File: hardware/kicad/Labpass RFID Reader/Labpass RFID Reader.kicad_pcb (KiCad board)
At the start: 2 copper layers, 74 x 74 mm, 59 parts, among them J1 Conn_01x03_Male, J2 Conn_01x08, J3 Conn_01x02, U1 adafruit_huzzah_32, U2 LM393, U3 LM324, U4 MFRC522, Y1 27.12 MHz

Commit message: Add terminal block for gpio to ext relay
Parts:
- added J4: Conn_01x02, Capstone Footprint Library:Anytek NQ, F.Cu at (154.6, 125.9)
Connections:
- net /Indicators/buzzer renamed /Indicators/BUZZER
- U1 pad 22: unconnected-(U1-Pad22) -> /Indicators/EXT_RELAY
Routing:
- net /Indicators/EXT_RELAY: track 0.00 -> 56.3 mm

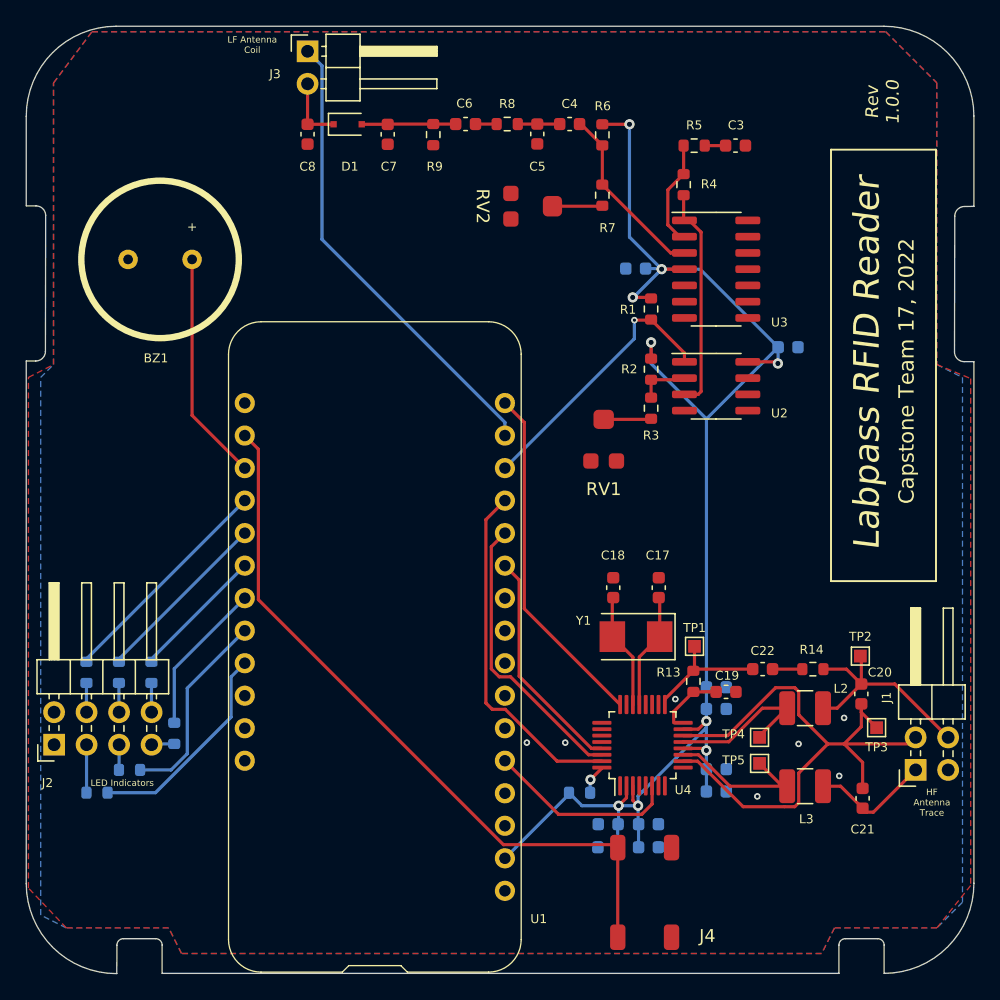
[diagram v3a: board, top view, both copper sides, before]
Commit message: Add back the mounting holes
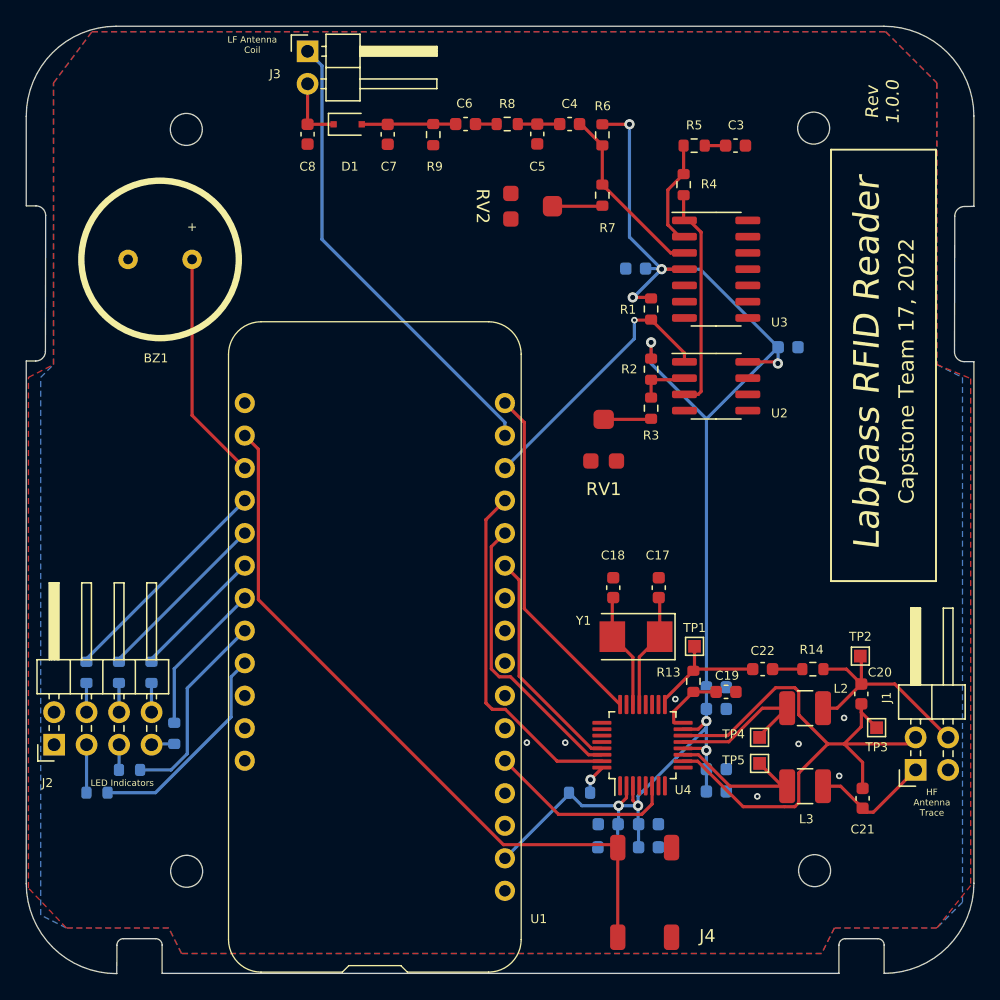
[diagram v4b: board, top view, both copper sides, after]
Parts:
- added REF**: MountingHole_2.5mm, MountingHole:MountingHole_2.5mm, F.Cu at (167.9, 124.2)
- added REF**: MountingHole_2.5mm, MountingHole:MountingHole_2.5mm, F.Cu at (118.8, 124.2)
- added REF**: MountingHole_2.5mm, MountingHole:MountingHole_2.5mm, F.Cu at (118.8, 66.3)
- added REF**: MountingHole_2.5mm, MountingHole:MountingHole_2.5mm, F.Cu at (167.8, 66.2)
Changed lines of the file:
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@@
     )
+  )
+  (footprint "MountingHole:MountingHole_2.5mm" (layer "F.Cu")
+    (at 167.875 124.2)
+    (descr "Mounting Hole 2.5mm, no annular")
+    (tags "mounting hole 2.5mm no annular")
+    (attr exclude_from_pos_files exclude_from_bom)
+    (fp_text reference "REF**" (at 0 -3.5) (layer "F.SilkS") hide
+      (effects (font (size 1 1) (thickness 0.15)))
+    )
+    (fp_text value "MountingHole_2.5mm" (at 0 3.5) (layer "F.Fab")
+      (effects (font (size 1 1) (thickness 0.15)))
+    )
+    (fp_text user "${REFERENCE}" (at 0 0) (layer "F.Fab")
+      (effects (font (size 1 1) (thickness 0.15)))
+    )
+    (fp_circle (center 0 0) (end 2.5 0) (layer "Cmts.User") (width 0.15) (fill none))
+    (fp_circle (center 0 0) (end 2.75 0) (layer "F.CrtYd") (width 0.05) (fill none))
+    (pad "" np_thru_hole circle (at 0 0) (size 2.5 2.5) (drill 2.5) (layers *.Cu *.Mask))
   )
   (footprint "Capstone Footprint Library:buzzer" (layer "F.Cu")
@@
     )
   )
+  (footprint "MountingHole:MountingHole_2.5mm" (layer "F.Cu")
+    (at 118.825 124.25)
+    (descr "Mounting Hole 2.5mm, no annular")
+    (tags "mounting hole 2.5mm no annular")
+    (attr exclude_from_pos_files exclude_from_bom)
+    (fp_text reference "REF**" (at 0 -3.5) (layer "F.SilkS") hide
+      (effects (font (size 1 1) (thickness 0.15)))
+    )
+    (fp_text value "MountingHole_2.5mm" (at 0 3.5) (layer "F.Fab")
+      (effects (font (size 1 1) (thickness 0.15)))
+    )
+    (fp_text user "${REFERENCE}" (at 0 0) (layer "F.Fab")
+      (effects (font (size 1 1) (thickness 0.15)))
+    )
+    (fp_circle (center 0 0) (end 2.5 0) (layer "Cmts.User") (width 0.15) (fill none))
+    (fp_circle (center 0 0) (end 2.75 0) (layer "F.CrtYd") (width 0.05) (fill none))
+    (pad "" np_thru_hole circle (at 0 0) (size 2.5 2.5) (drill 2.5) (layers *.Cu *.Mask))
+  )
   (footprint "Capstone Footprint Library:Anytek NQ" (layer "F.Cu")
     (at 154.6 125.9 -90)
@@
       (rotate (xyz 0 0 0))
     )
+  )
+  (footprint "MountingHole:MountingHole_2.5mm" (layer "F.Cu")
+    (at 118.8 66.3)
+    (descr "Mounting Hole 2.5mm, no annular")
+    (tags "mounting hole 2.5mm no annular")
+    (attr exclude_from_pos_files exclude_from_bom)
+    (fp_text reference "REF**" (at 0 -3.5) (layer "F.SilkS") hide
+      (effects (font (size 1 1) (thickness 0.15)))
+    )
+    (fp_text value "MountingHole_2.5mm" (at 0 3.5) (layer "F.Fab")
+      (effects (font (size 1 1) (thickness 0.15)))
+    )
+    (fp_text user "${REFERENCE}" (at 0 0) (layer "F.Fab")
+      (effects (font (size 1 1) (thickness 0.15)))
+    )
+    (fp_circle (center 0 0) (end 2.5 0) (layer "Cmts.User") (width 0.15) (fill none))
+    (fp_circle (center 0 0) (end 2.75 0) (layer "F.CrtYd") (width 0.05) (fill none))
+    (pad "" np_thru_hole circle (at 0 0) (size 2.5 2.5) (drill 2.5) (layers *.Cu *.Mask))
   )
   (footprint "Resistor_SMD:R_0603_1608Metric" (layer "F.Cu")
@@
       (net 29 "/labpass_rf_13.56M/TX1") (pinfunction "1") (pintype "passive"))
   )
+  (footprint "MountingHole:MountingHole_2.5mm" (layer "F.Cu")
+    (at 167.8 66.2)
+    (descr "Mounting Hole 2.5mm, no annular")
+    (tags "mounting hole 2.5mm no annular")
+    (attr exclude_from_pos_files exclude_from_bom)
+    (fp_text reference "REF**" (at 0 -3.5) (layer "F.SilkS") hide
+      (effects (font (size 1 1) (thickness 0.15)))
+    )
+    (fp_text value "MountingHole_2.5mm" (at 0 3.5) (layer "F.Fab")
+      (effects (font (size 1 1) (thickness 0.15)))
+    )
+    (fp_text user "${REFERENCE}" (at 0 0) (layer "F.Fab")
+      (effects (font (size 1 1) (thickness 0.15)))
+    )
+    (fp_circle (center 0 0) (end 2.5 0) (layer "Cmts.User") (width 0.15) (fill none))
+    (fp_circle (center 0 0) (end 2.75 0) (layer "F.CrtYd") (width 0.05) (fill none))
+    (pad "" np_thru_hole circle (at 0 0) (size 2.5 2.5) (drill 2.5) (layers *.Cu *.Mask))
+  )
   (footprint "Capacitor_SMD:C_0603_1608Metric" (layer "F.Cu")
